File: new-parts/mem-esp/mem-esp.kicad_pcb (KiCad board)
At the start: 2 copper layers, 134.6 x 49.5 mm, 70 parts, among them J1 Conn_02x02_Odd_Even, J2 BHR-10-VUA, J3 BHR-10-VUA, J4 Conn_01x01, J5 Conn_01x01, J6 Conn_01x01, J7 Conn_01x01, J8 BHR-10-VUA, U1 BA7806CP-E2, U2 ESP32-S3-DevKitC, U3 LTV-247, U4 LTV-247, U5 DRV8908, U6 LTV-247, U7 LTV-247, U8 LTV-247, U9 DRV8908

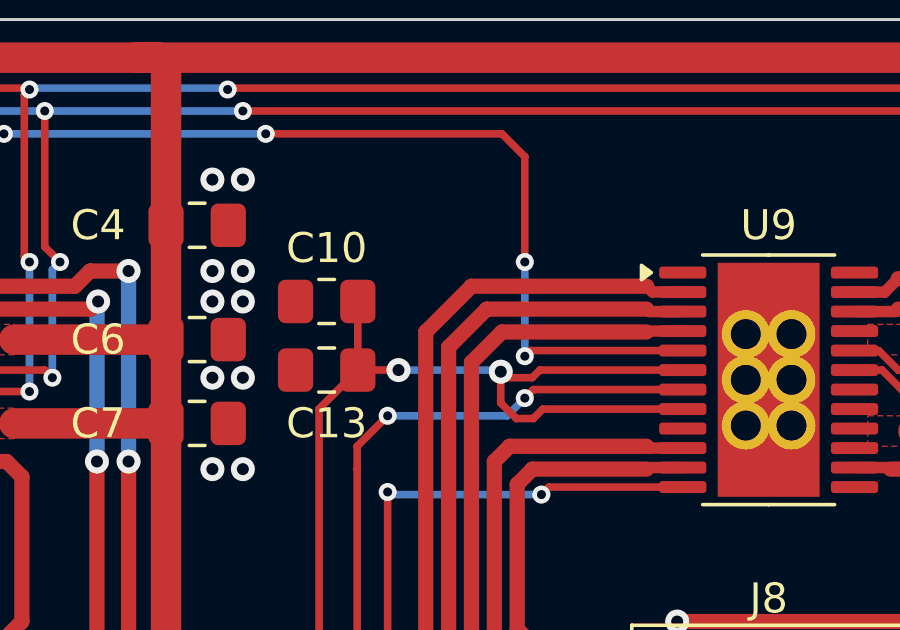
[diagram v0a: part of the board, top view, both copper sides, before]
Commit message: mem-esp: Add solder jumper to connect SPI if the second driver is not populated.
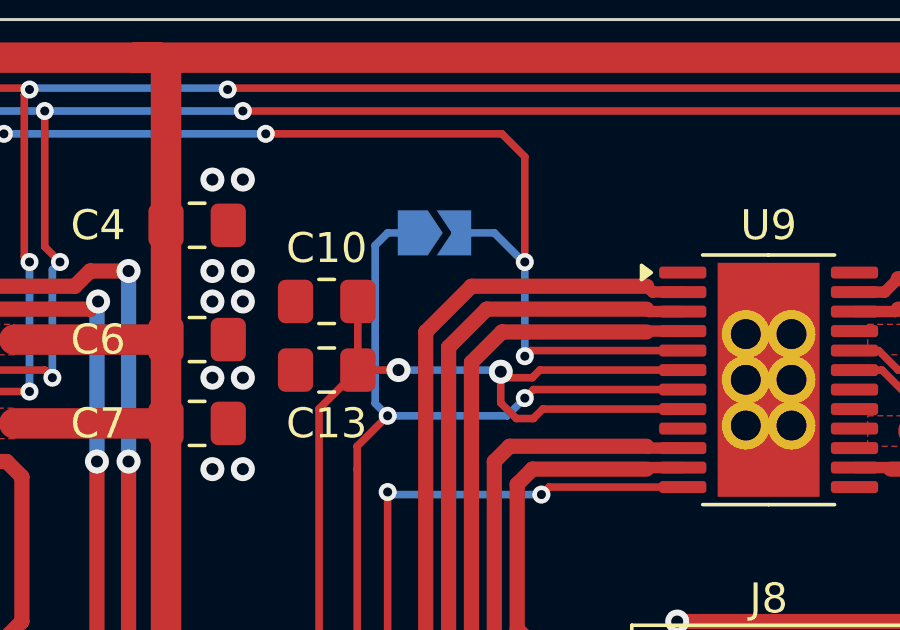
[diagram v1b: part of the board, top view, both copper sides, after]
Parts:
- added JP4: SolderJumper_2_Open, Jumper:SolderJumper-2_P1.3mm_Open_TrianglePad1.0x1.5mm, B.Cu at (216.2, 78.2)
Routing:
- net /sdi3: track 106.1 -> 113.3 mm
- net /sdi2: track 60.0 -> 62.6 mm
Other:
- board text added: "close if no U9"
